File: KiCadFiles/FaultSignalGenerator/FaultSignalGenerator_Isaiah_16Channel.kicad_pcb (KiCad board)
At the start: 2 copper layers, 280 parts, among them J1 Conn_02x20_Odd_Even, J2 Conn_02x16_Odd_Even, J3 DB25_Receptacle, U1 MCP4431-503E/ST, U10 TL074CDR, U11 TL074CDR, U12 TL074CDR, U13 TL074CDR, U14 PCM1681PWP, U15 PCM1681PWP, U16 TL780-05CKTTR, U2 MCP4431-503E/ST, U3 MCP4431-503E/ST, U4 MCP4431-503E/ST, U5 TL074CDR, U6 TL074CDR, U7 TL074CDR, U8 TL074CDR, U9 TL074CDR

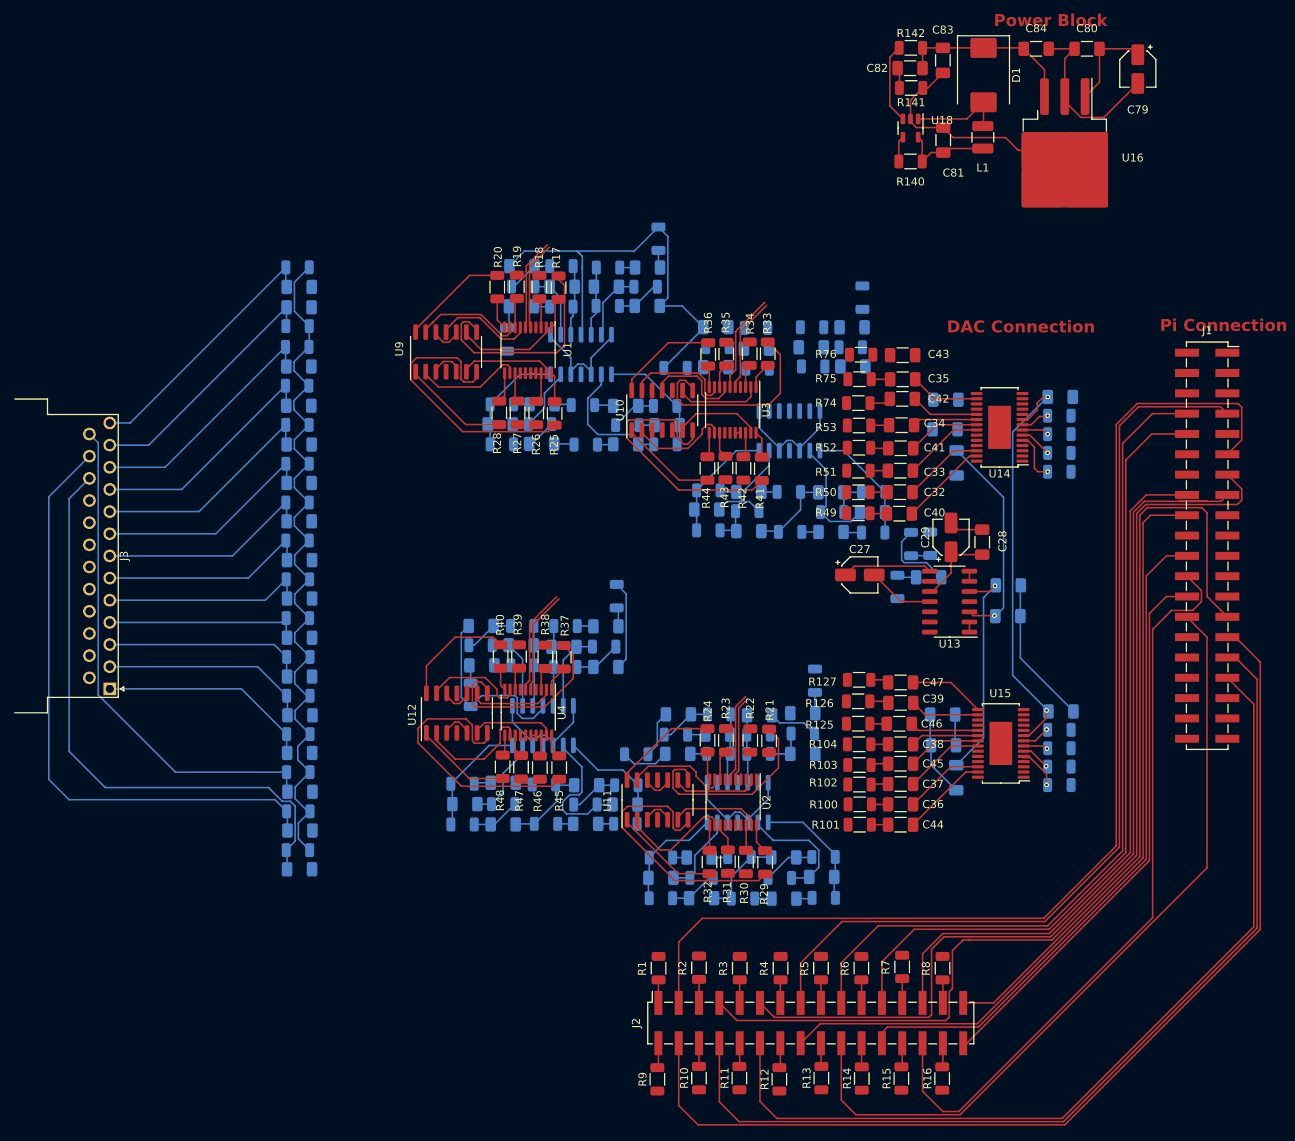
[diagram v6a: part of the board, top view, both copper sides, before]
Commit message: PCB Work
Connected F and B sides, created internal layers, started connecting those together.
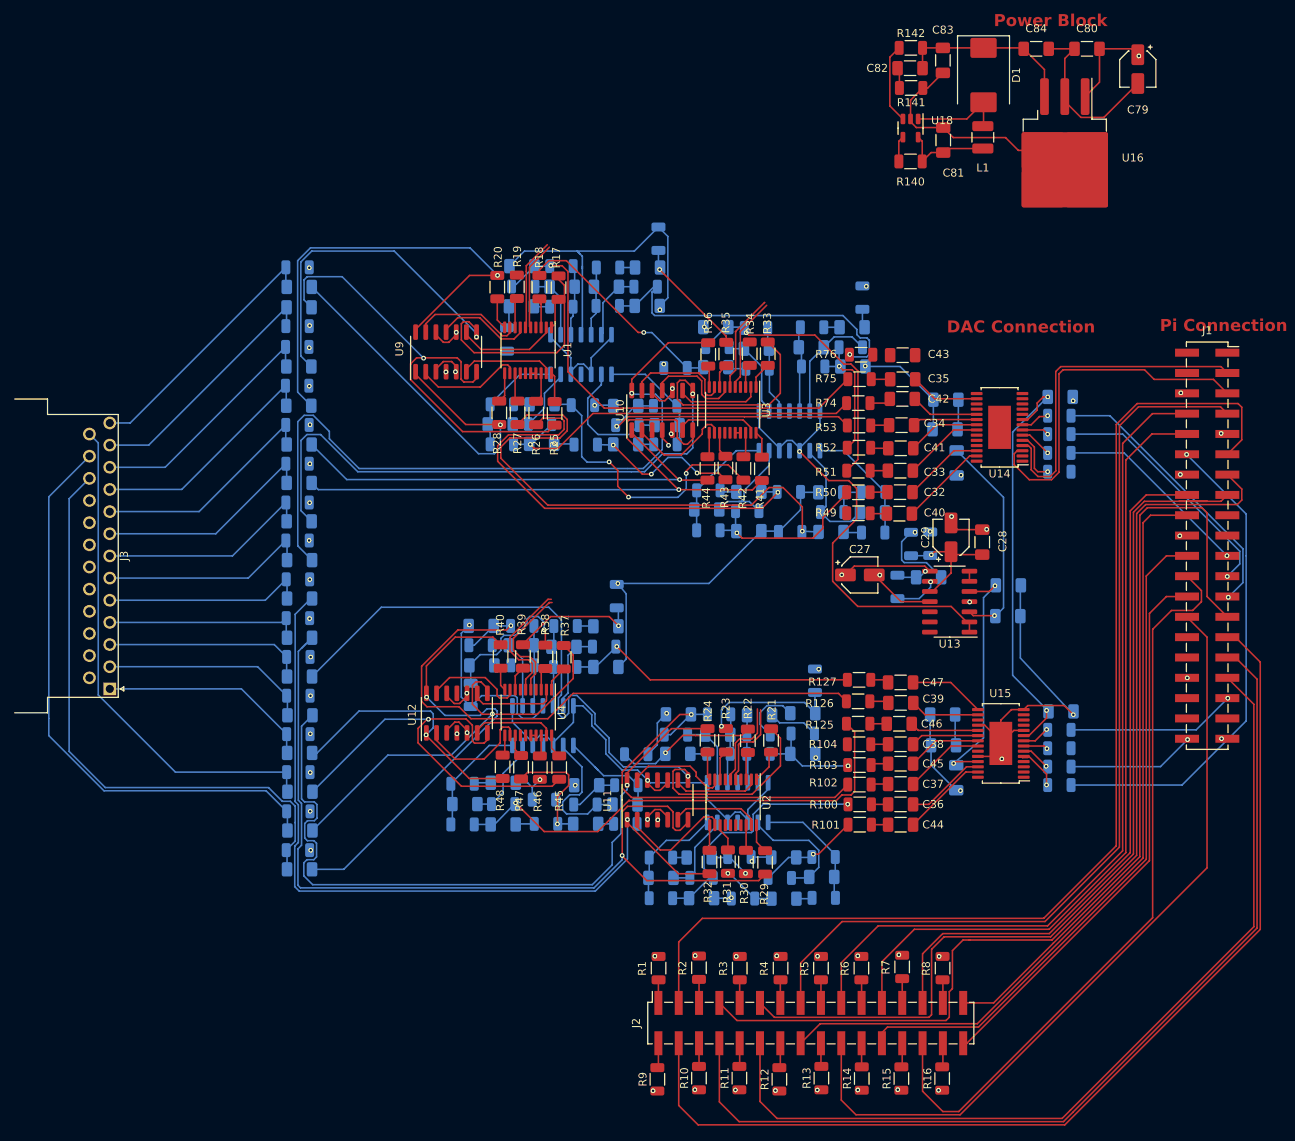
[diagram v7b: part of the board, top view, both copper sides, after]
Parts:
- moved R137 1.91 mm to (196.5, 114.3)
- moved R39 0.49 mm to (193.9, 96.4)
- moved R22 0.30 mm to (222.0, 106.9)
- moved R21 0.25 mm to (224.9, 106.9)
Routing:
- net 0: track 356.6 -> 924.2 mm, vias 0 -> 62
- net +12V: track 11.8 -> 363.1 mm, vias 0 -> 7
- net +6V: track 38.0 -> 208.0 mm, vias 0 -> 10
- net Channel9: track 13.3 -> 99.1 mm, vias 0 -> 1
- net Channel8: track 12.9 -> 92.0 mm, vias 0 -> 1
- net Channel10: track 34.6 -> 112.1 mm, vias 0 -> 1
- net Channel12: track 13.2 -> 89.5 mm, vias 0 -> 1
- net Net-(C71-Pad1): track 6.21 -> 80.0 mm, vias 0 -> 1
- net Channel11: track 25.3 -> 97.5 mm, vias 0 -> 1
- net Channel7: track 25.7 -> 95.5 mm, vias 0 -> 1
- net gain1: track 2.09 -> 66.1 mm, vias 0 -> 1
- net TDMB_SCK: track 0.00 -> 61.6 mm, vias 0 -> 1
- net Net-(C70-Pad1): track 6.13 -> 61.3 mm, vias 0 -> 1
- net gain2: track 1.98 -> 56.6 mm, vias 0 -> 1
- net Net-(C18-Pad1): track 5.83 -> 59.7 mm, vias 0 -> 1
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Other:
- copper layers 2 -> 4

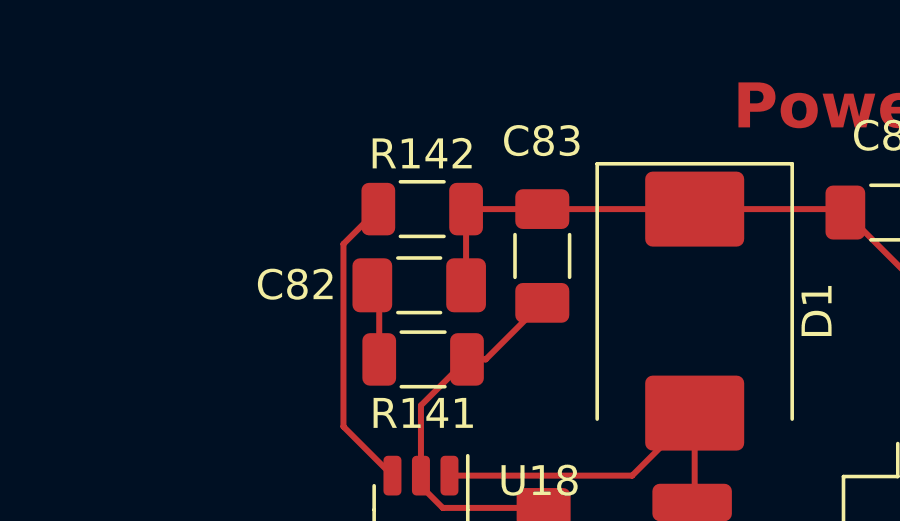
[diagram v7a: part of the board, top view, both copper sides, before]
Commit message: Changed 138.1k resistor size
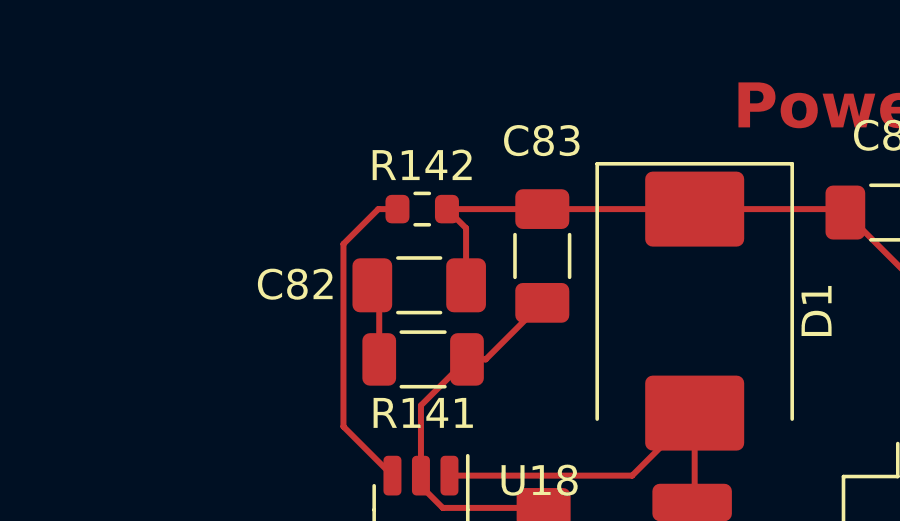
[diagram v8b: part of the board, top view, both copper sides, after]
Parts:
- R142: footprint Resistor_SMD:R_1206_3216Metric -> Resistor_SMD:R_0603_1608Metric
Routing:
- net Net-(D1-K): track 22.3 -> 23.2 mm
- net Net-(U18-FB): track 10.0 -> 10.7 mm
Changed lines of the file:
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@@
     )
   )
-  (footprint "Resistor_SMD:R_1206_3216Metric" (layer "F.Cu")
+  (footprint "Resistor_SMD:R_0603_1608Metric" (layer "F.Cu")
     (at 242.3775 20.32)
-    (descr "Resistor SMD 1206 (3216 Metric), square (rectangular) end terminal, IPC_7351 nominal, (Body size source: IPC-SM-782 page 72, https://www.pcb-3d.com/wordpress/wp-content/uploads/ipc-sm-782a_amendment_1_and_2.pdf), generated with kicad-footprint-generator")
+    (descr "Resistor SMD 0603 (1608 Metric), square (rectangular) end terminal, IPC_7351 nominal, (Body size source: IPC-SM-782 page 72, https://www.pcb-3d.com/wordpress/wp-content/uploads/ipc-sm-782a_amendment_1_and_2.pdf), generated with kicad-footprint-generator")
     (tags "resistor")
     (property "Sheetfile" "power.kicad_sch")
@@
     (property "ki_keywords" "R res resistor")
     (attr smd)
-    (fp_text reference "R142" (at 0 -1.82) (layer "F.SilkS")
+    (fp_text reference "R142" (at 0 -1.43) (layer "F.SilkS")
         (effects (font (size 1 1) (thickness 0.15)))
     )
-    (fp_text value "138.1k" (at 0 1.82) (layer "F.Fab")
+    (fp_text value "138.1k" (at 0 1.43) (layer "F.Fab")
         (effects (font (size 1 1) (thickness 0.15)))
     )
-    (fp_text user "${REFERENCE}" (at 0 -0.8) (layer "F.Fab")
-        (effects (font (size 0.8 0.8) (thickness 0.12)))
+    (fp_text user "${REFERENCE}" (at 0 0) (layer "F.Fab")
+        (effects (font (size 0.4 0.4) (thickness 0.06)))
     )
-    (fp_line (start -0.727064 -0.91) (end 0.727064 -0.91)
+    (fp_line (start -0.237258 -0.5225) (end 0.237258 -0.5225)
       (stroke (width 0.12) (type solid)) (layer "F.SilkS"))
-    (fp_line (start -0.727064 0.91) (end 0.727064 0.91)
+    (fp_line (start -0.237258 0.5225) (end 0.237258 0.5225)
       (stroke (width 0.12) (type solid)) (layer "F.SilkS"))
-    (fp_line (start -2.28 -1.12) (end 2.28 -1.12)
+    (fp_line (start -1.48 -0.73) (end 1.48 -0.73)
       (stroke (width 0.05) (type solid)) (layer "F.CrtYd"))
-    (fp_line (start -2.28 1.12) (end -2.28 -1.12)
+    (fp_line (start -1.48 0.73) (end -1.48 -0.73)
       (stroke (width 0.05) (type solid)) (layer "F.CrtYd"))
-    (fp_line (start 2.28 -1.12) (end 2.28 1.12)
+    (fp_line (start 1.48 -0.73) (end 1.48 0.73)
       (stroke (width 0.05) (type solid)) (layer "F.CrtYd"))
-    (fp_line (start 2.28 1.12) (end -2.28 1.12)
+    (fp_line (start 1.48 0.73) (end -1.48 0.73)
       (stroke (width 0.05) (type solid)) (layer "F.CrtYd"))
-    (fp_line (start -1.6 -0.8) (end 1.6 -0.8)
+    (fp_line (start -0.8 -0.4125) (end 0.8 -0.4125)
       (stroke (width 0.1) (type solid)) (layer "F.Fab"))
-    (fp_line (start -1.6 0.8) (end -1.6 -0.8)
+    (fp_line (start -0.8 0.4125) (end -0.8 -0.4125)
       (stroke (width 0.1) (type solid)) (layer "F.Fab"))
-    (fp_line (start 1.6 -0.8) (end 1.6 0.8)
+    (fp_line (start 0.8 -0.4125) (end 0.8 0.4125)
       (stroke (width 0.1) (type solid)) (layer "F.Fab"))
-    (fp_line (start 1.6 0.8) (end -1.6 0.8)
+    (fp_line (start 0.8 0.4125) (end -0.8 0.4125)
       (stroke (width 0.1) (type solid)) (layer "F.Fab"))
-    (pad "1" smd roundrect (at -1.4625 0) (size 1.125 1.75) (layers "F.Cu" "F.Paste" "F.Mask") (roundrect_rratio 0.222222)
+    (pad "1" smd roundrect (at -0.825 0) (size 0.8 0.95) (layers "F.Cu" "F.Paste" "F.Mask") (roundrect_rratio 0.25)
       (net 55 "Net-(U18-FB)") (pintype "passive"))
-    (pad "2" smd roundrect (at 1.4625 0) (size 1.125 1.75) (layers "F.Cu" "F.Paste" "F.Mask") (roundrect_rratio 0.222222)
+    (pad "2" smd roundrect (at 0.825 0) (size 0.8 0.95) (layers "F.Cu" "F.Paste" "F.Mask") (roundrect_rratio 0.25)
       (net 56 "Net-(D1-K)") (pintype "passive"))
-    (model "${KICAD6_3DMODEL_DIR}/Resistor_SMD.3dshapes/R_1206_3216Metric.wrl"
+    (model "${KICAD6_3DMODEL_DIR}/Resistor_SMD.3dshapes/R_0603_1608Metric.wrl"
       (offset (xyz 0 0 0))
       (scale (xyz 1 1 1))
@@
   (segment (start 240.915 20.32) (end 239.7525 21.4825) (width 0.2) (layer "F.Cu") (net 55))
   (segment (start 239.7525 27.571149) (end 241.385776 29.204425) (width 0.2) (layer "F.Cu") (net 55))
-  (segment (start 243.84 20.32) (end 243.84 22.86) (width 0.2) (layer "F.Cu") (net 56))
+  (segment (start 240.915 20.32) (end 241.5525 20.32) (width 0.2) (layer "F.Cu") (net 55))
   (segment (start 251.46 20.32) (end 246.38 20.32) (width 0.2) (layer "F.Cu") (net 56))
   (segment (start 259.08 23.0325) (end 256.4825 20.435) (width 0.2) (layer "F.Cu") (net 56))
   (segment (start 259.08 26.41) (end 259.08 23.0325) (width 0.2) (layer "F.Cu") (net 56))
+  (segment (start 243.84 20.9575) (end 243.84 22.86) (width 0.2) (layer "F.Cu") (net 56))
   (segment (start 256.3675 20.32) (end 251.46 20.32) (width 0.2) (layer "F.Cu") (net 56))
-  (segment (start 246.38 20.32) (end 243.84 20.32) (width 0.2) (layer "F.Cu") (net 56))
+  (segment (start 246.38 20.32) (end 243.2025 20.32) (width 0.2) (layer "F.Cu") (net 56))
+  (segment (start 243.2025 20.32) (end 243.84 20.9575) (width 0.2) (layer "F.Cu") (net 56))
   (segment (start 256.4825 20.435) (end 256.3675 20.32) (width 0.2) (layer "F.Cu") (net 56))
   (segment (start 219.3 57.125) (end 219.3 56.362117) (width 0.2) (layer "F.Cu") (net 57))
